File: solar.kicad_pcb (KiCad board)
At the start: 2 copper layers, 78.5 x 148 mm, 11 parts

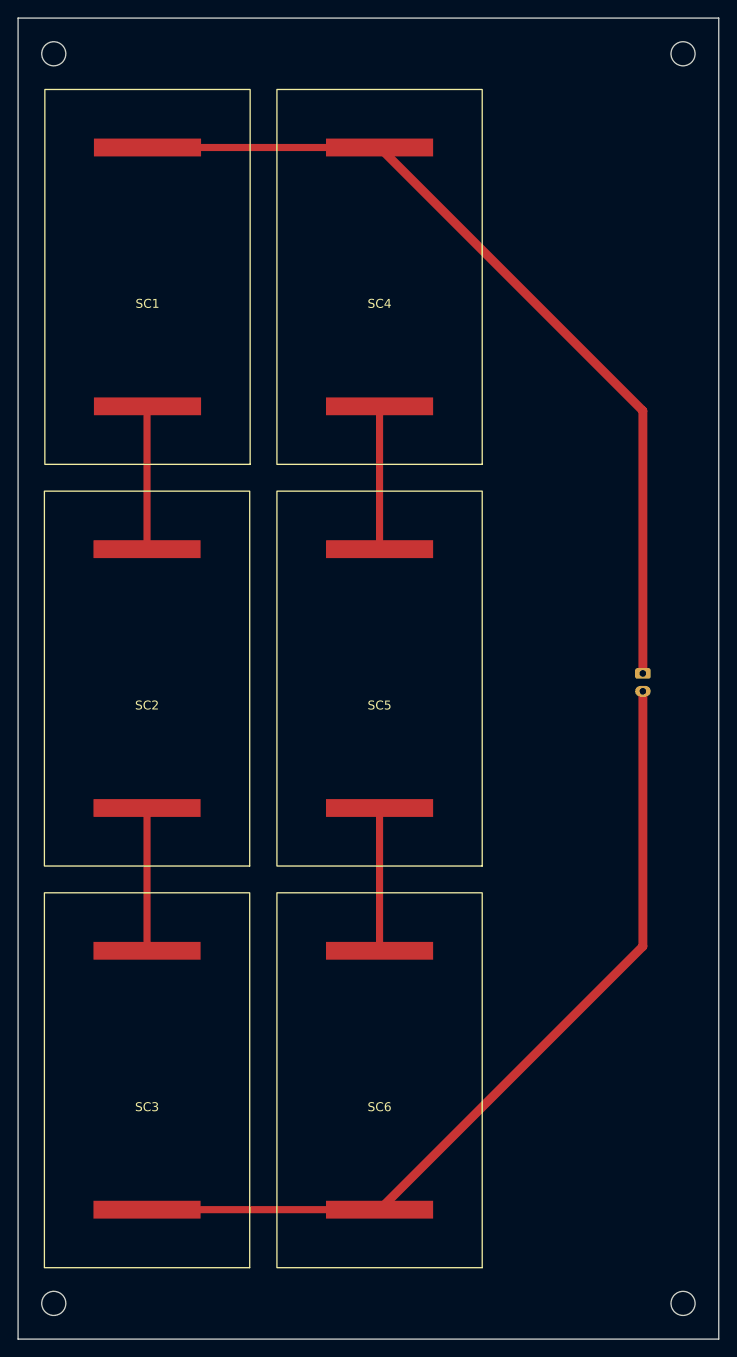
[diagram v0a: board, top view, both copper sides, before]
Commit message: add temperature sensor
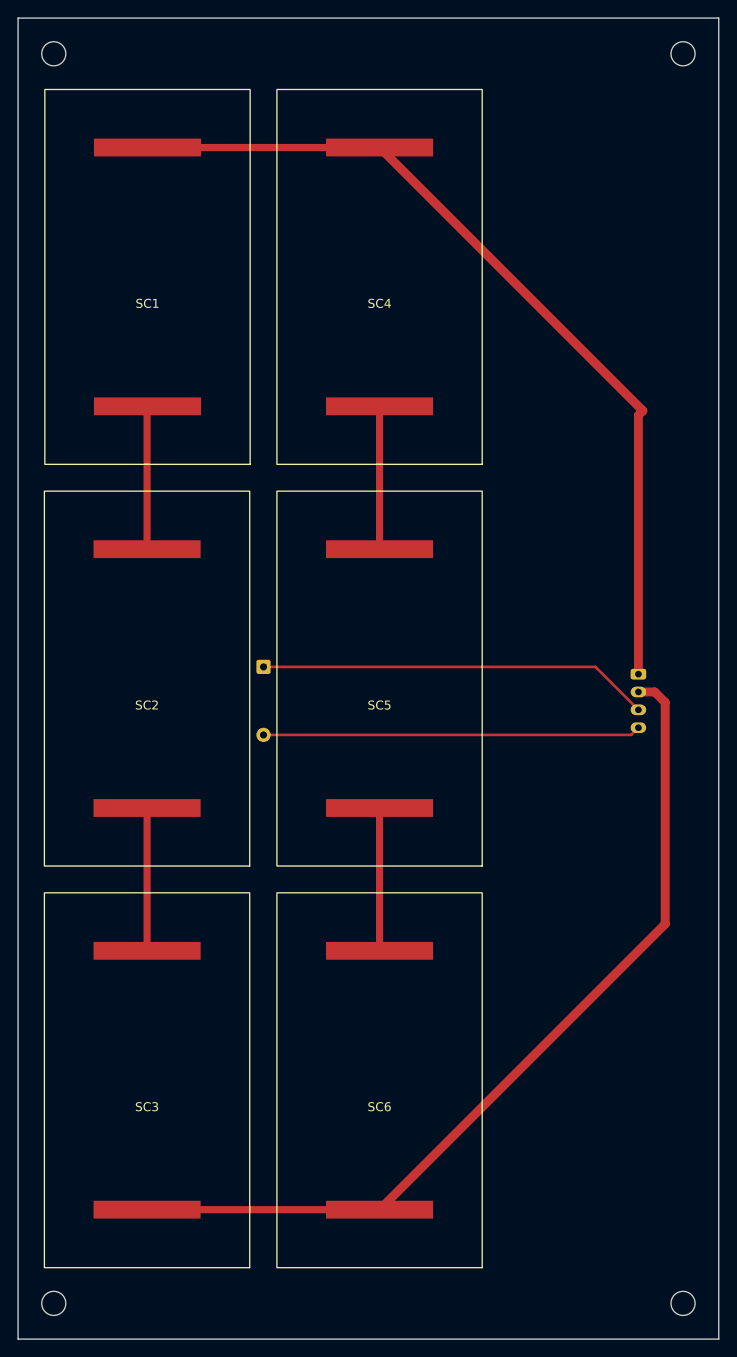
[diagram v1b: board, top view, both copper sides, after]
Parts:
- removed J_SOLAR_OUT1: Conn_01x02, Connector_JST:JST_PH_S2B-PH-K_1x02_P2.00mm_Horizontal
- added J_SOLOAR_OUT_1: Conn_01x04, Connector_JST:JST_PH_S4B-PH-K_1x04_P2.00mm_Horizontal, B.Cu at (119.5, 93.5)
- added TH1: 10K NTC, Diode_THT:D_DO-35_SOD27_P7.62mm_Horizontal, B.Cu at (77.5, 92.7)
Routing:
- net /TEMP_SENSE: track 0.00 -> 44.0 mm
- net /TEMP_RETURN: track 0.00 -> 42.3 mm
- net /SOLAR-: track 96.3 -> 99.6 mm
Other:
- board text added: "TR"
- board text added: "TS"
